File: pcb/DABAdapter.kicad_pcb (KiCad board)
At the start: 2 copper layers, 27 x 58.5 mm, 31 parts, among them J1 RFShield_OnePiece, J2 Ant, J3 Conn_01x06, J4 AudioJack3_Ground, J6 Conn_01x06, U3 abcdefg, U4 MIC5504-1.8YM5, Y1 19.2Mhz

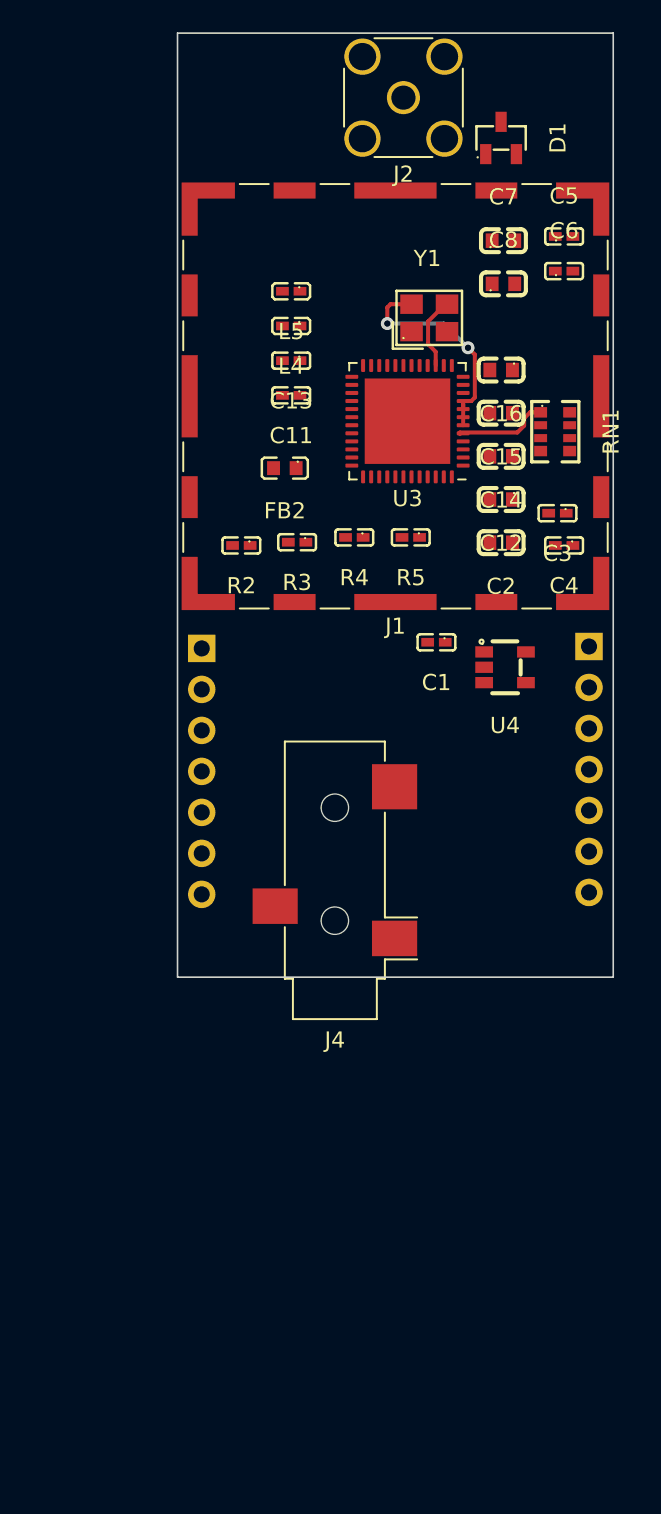
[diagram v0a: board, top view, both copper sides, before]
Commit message: Add flash chip to the layout
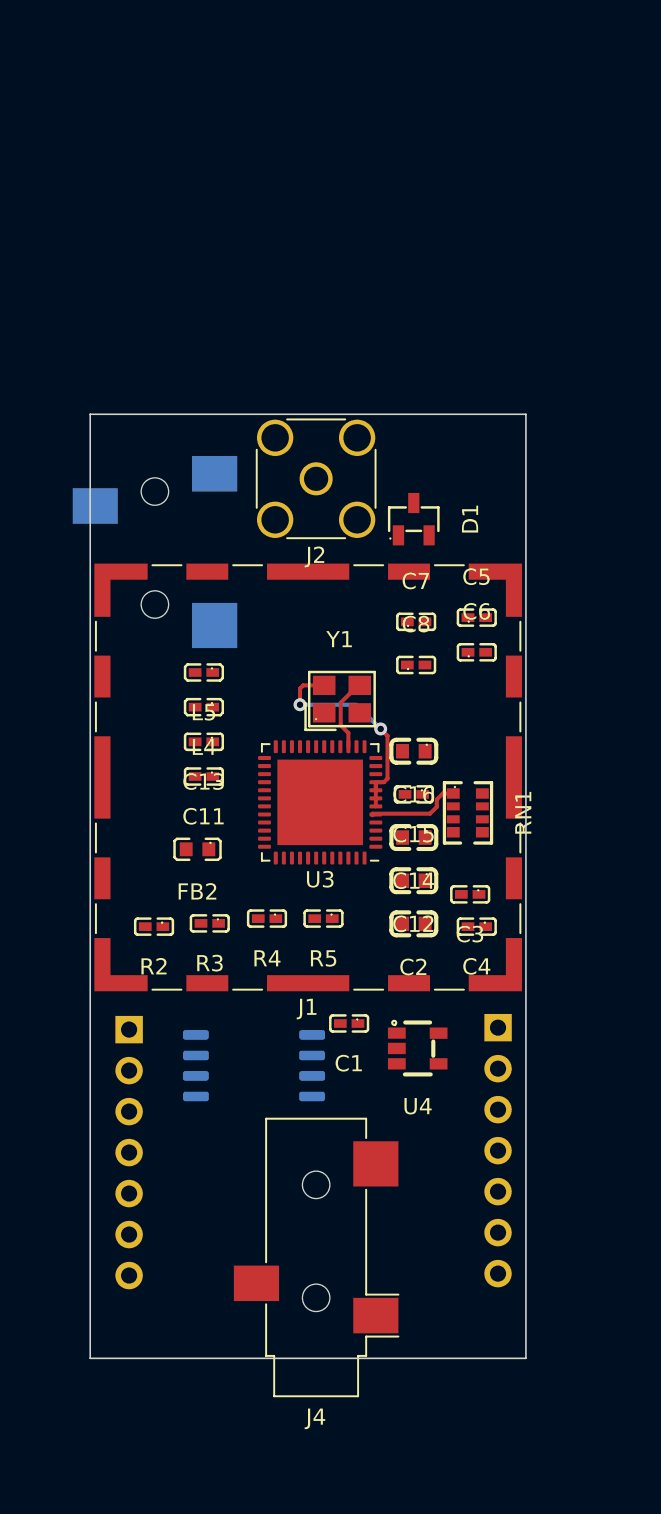
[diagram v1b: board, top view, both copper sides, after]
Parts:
- added J5: TRS Antenna, Connector_Audio:Jack_3.5mm_CUI_SJ-3523-SMT_Horizontal, B.Cu at (101.6, 69.2)
- added U1: SST25VF080B-50-4x-S2Ax, Package_SO:SOIC-8_5.275x5.275mm_P1.27mm, B.Cu at (107.7, 102.2)
- C15, C7, C8: footprint jlc_footprints:C0603 -> jlc_footprints:C0402
- moved J6 24.3 mm to (122.9, 99.9)
- moved C1 24.2 mm to (113.6, 99.6)
- moved C13 24.2 mm to (104.6, 82.2)
- moved C14 24.2 mm to (117.6, 88.1)
- moved C15 24.2 mm to (117.6, 85.4)
- moved C2 24.2 mm to (117.6, 93.4)
- moved C3 24.2 mm to (121.1, 91.6)
- moved C4 24.2 mm to (121.5, 93.6)
- moved C6 24.2 mm to (121.5, 76.6)
- moved D1 24.2 mm to (117.6, 68.4)
- moved J2 24.2 mm to (111.6, 65.9)
- moved L5 24.2 mm to (104.6, 77.9)
- moved R2 24.2 mm to (101.5, 93.6)
- moved R3 24.2 mm to (105.0, 93.4)
- moved R4 24.2 mm to (108.5, 93.1)
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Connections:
- net Net-(J2-In) renamed ANT

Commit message: Routing of the pcb
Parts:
- removed J5: TRS Antenna, Connector_Audio:Jack_3.5mm_CUI_SJ-3523-SMT_Horizontal
- removed RN1: 10k, jlc_footprints:RES-ARRAY-SMD_0603-8P-L3.2-W1.6-BL
- added R1: 10k, jlc_footprints:C0402, F.Cu at (117.7, 73.8)
- added R6: 10k, jlc_footprints:C0402, F.Cu at (122.0, 84.4)
- added R7: 10k, jlc_footprints:C0402, F.Cu at (115.6, 74.1)
- added R8: 10k, jlc_footprints:C0402, F.Cu at (115.7, 72.9)
- moved U1 27.1 mm to (115.6, 76.3), turned to 90 degrees
- moved U4 26.9 mm to (120.2, 74.4), turned to 90 degrees
- moved R2 17.9 mm to (118.6, 88.0), turned to -45 degrees
- moved C3 17.9 mm to (122.6, 73.8), turned to -90 degrees
- moved C5 17.1 mm to (111.7, 88.5), turned to 90 degrees
- moved C4 16.6 mm to (121.4, 77.0), turned to 0 degrees
- moved R3 15.8 mm to (119.5, 87.2), turned to -45 degrees
- moved J3 15.1 mm to (99.5, 115.1), turned to 0 degrees
- moved C1 14.7 mm to (110.2, 85.4), turned to 90 degrees
- moved C7 14.6 mm to (113.0, 88.5), turned to 90 degrees
- moved C6 14.0 mm to (114.3, 88.5), turned to 90 degrees
- moved R4 13.6 mm to (120.4, 86.4), turned to -45 degrees
- moved C8 13.3 mm to (110.5, 88.5), turned to 90 degrees
- moved C15 12.2 mm to (106.2, 81.2), turned to 90 degrees
- moved C2 12.1 mm to (121.4, 81.9)
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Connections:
- J3 pad 3: SMODE -> ROUT
- J3 pad 4: INTB -> LOUT
- J3 pad 5: RSTB -> INTB
- J3 pad 6: LOUT -> RSTB
- J3 pad 7: ROUT -> SMODE
- J6 pad 3: SPI_SSB -> SPI_SCLK
- J6 pad 4: SPI_SCLK -> SPI_SSB
- J6 pad 5: I2S_DCLK -> I2S_DFS
- J6 pad 6: I2S_DFS -> I2S_DCLK
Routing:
- net INTB: track 0.10 -> 54.5 mm, vias 0 -> 3
- net +3V3: track 0.00 -> 46.9 mm, vias 0 -> 6
- net RSTB: track 0.00 -> 43.6 mm, vias 0 -> 2
- net LOUT: track 0.00 -> 39.6 mm, vias 0 -> 2
- net ROUT: track 0.00 -> 37.8 mm
- net I2S_DATA: track 0.00 -> 37.3 mm
- net SMODE: track 5.89 -> 41.7 mm, vias 0 -> 2
- net I2S_DCLK: track 0.00 -> 31.6 mm
- net I2S_DFS: track 0.00 -> 29.3 mm
- net GND: track 14.1 -> 40.3 mm, vias 2 -> 34
- net SPI_SSB: track 0.00 -> 22.8 mm
- net +1V8: track 0.00 -> 21.7 mm, vias 0 -> 2
- net SPI_SCLK: track 0.00 -> 17.9 mm
- net SPI_MOSI: track 0.00 -> 16.4 mm
- net SPI_MISO: track 0.00 -> 14.8 mm
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- added copper zone on F.Cu, net +1V8
- added copper zone on F.Cu, net +3V3
- added copper zone on B.Cu, net GND
- added copper zone on F.Cu, net GND

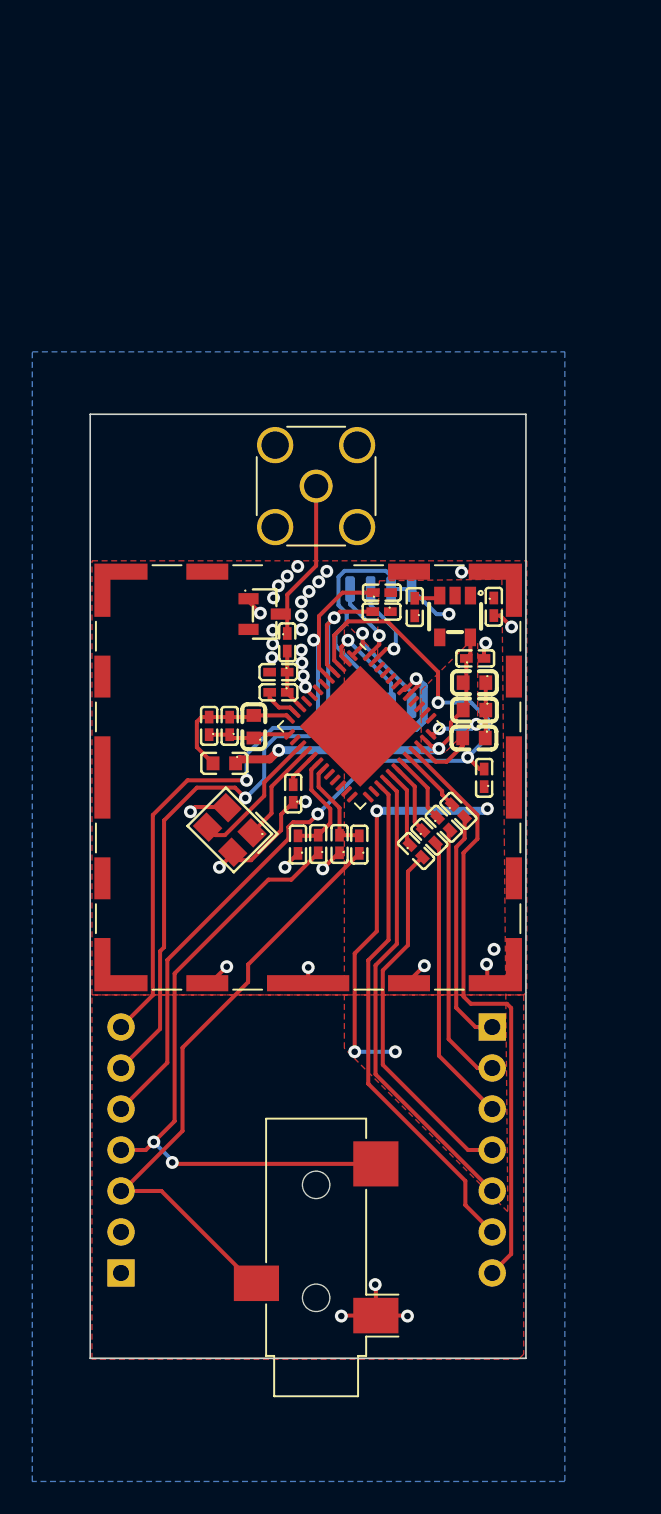
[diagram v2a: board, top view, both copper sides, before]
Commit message: DRC and add step file of QFN package
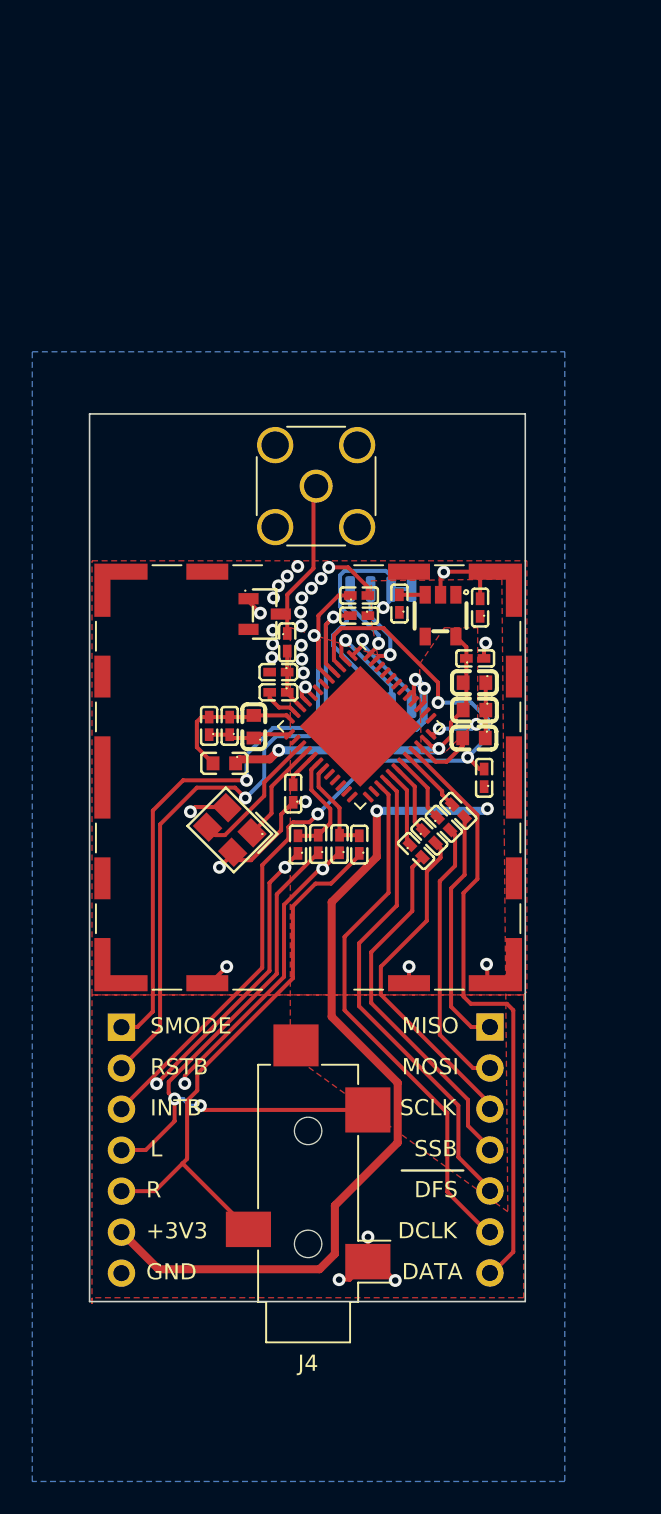
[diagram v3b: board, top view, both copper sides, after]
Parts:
- J4: footprint Connector_Audio:Jack_3.5mm_CUI_SJ-3523-SMT_Horizontal -> Connector_Audio:Jack_3.5mm_CUI_SJ-3524-SMT_Horizontal
- moved J3 15.2 mm to (99.5, 99.8), turned to 180 degrees
- moved J4 3.38 mm to (111.1, 110.8)
- moved R8 1.43 mm to (114.2, 73.1)
- moved R7 1.42 mm to (114.2, 74.3)
- moved R1 0.97 mm to (116.8, 73.6)
- moved U4 0.90 mm to (119.3, 74.3)
- moved C3 0.85 mm to (121.8, 73.8), turned to 90 degrees
- moved J6 0.14 mm to (122.4, 99.8)
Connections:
- J3 pad 1: GND -> SMODE
- J3 pad 2: +3V3 -> RSTB
- J3 pad 3: ROUT -> INTB
- J3 pad 5: INTB -> ROUT
- J3 pad 6: RSTB -> +3V3
- J3 pad 7: SMODE -> GND
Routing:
- net GND: track 40.3 -> 81.4 mm, vias 34 -> 35
- net +3V3: track 46.9 -> 73.7 mm, vias 6 -> 3
- net ROUT: track 37.8 -> 34.6 mm
- net SPI_SCLK: track 17.9 -> 21.0 mm
- net LOUT: track 39.6 -> 36.9 mm
- net I2S_DCLK: track 31.6 -> 33.0 mm
- net RSTB: track 43.6 -> 42.2 mm
- net SPI_MOSI: track 16.4 -> 17.3 mm
- net I2S_DFS: track 29.3 -> 30.1 mm
- net NVSSB: track 7.36 -> 6.55 mm
- net INTB: track 54.5 -> 53.8 mm
- net SMODE: track 41.7 -> 42.3 mm
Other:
- board size 27 x 58.5 mm -> 27 x 55 mm

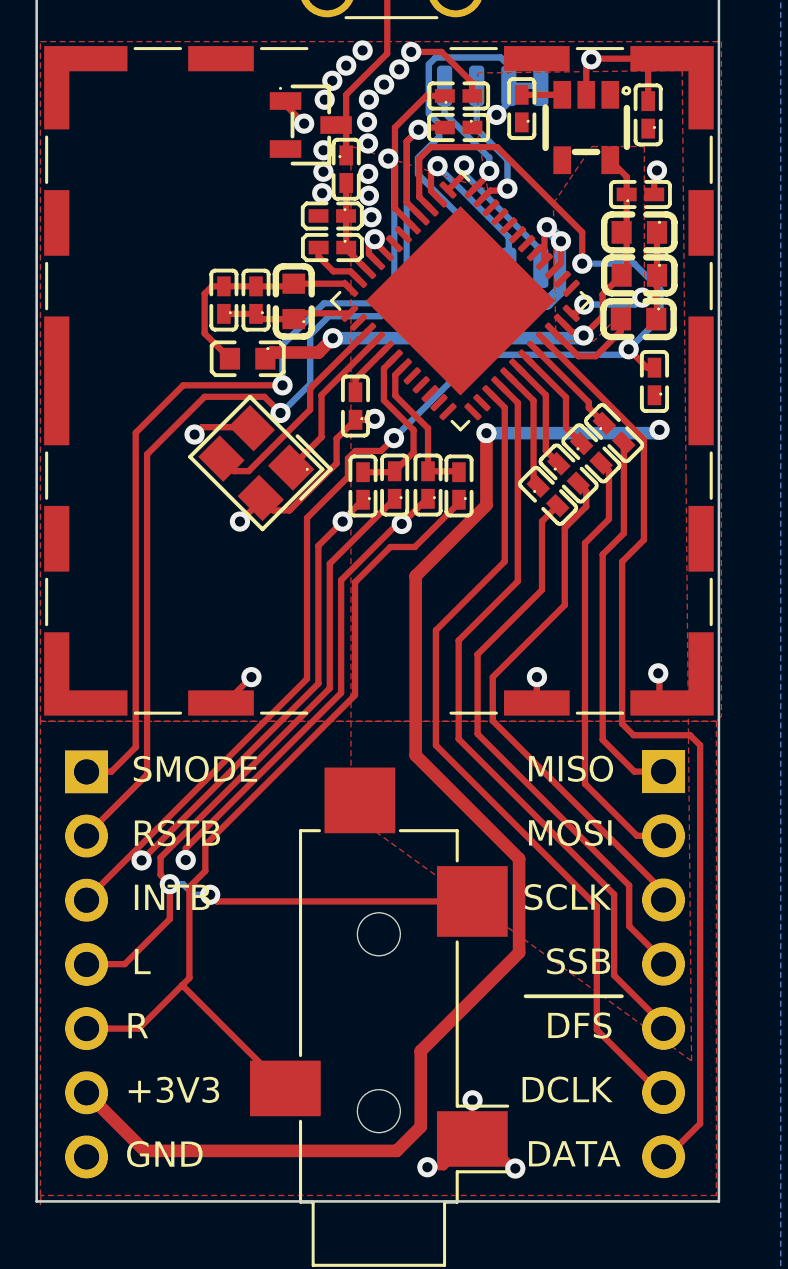
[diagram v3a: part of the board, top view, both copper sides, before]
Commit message: Rename FS to RLCLK
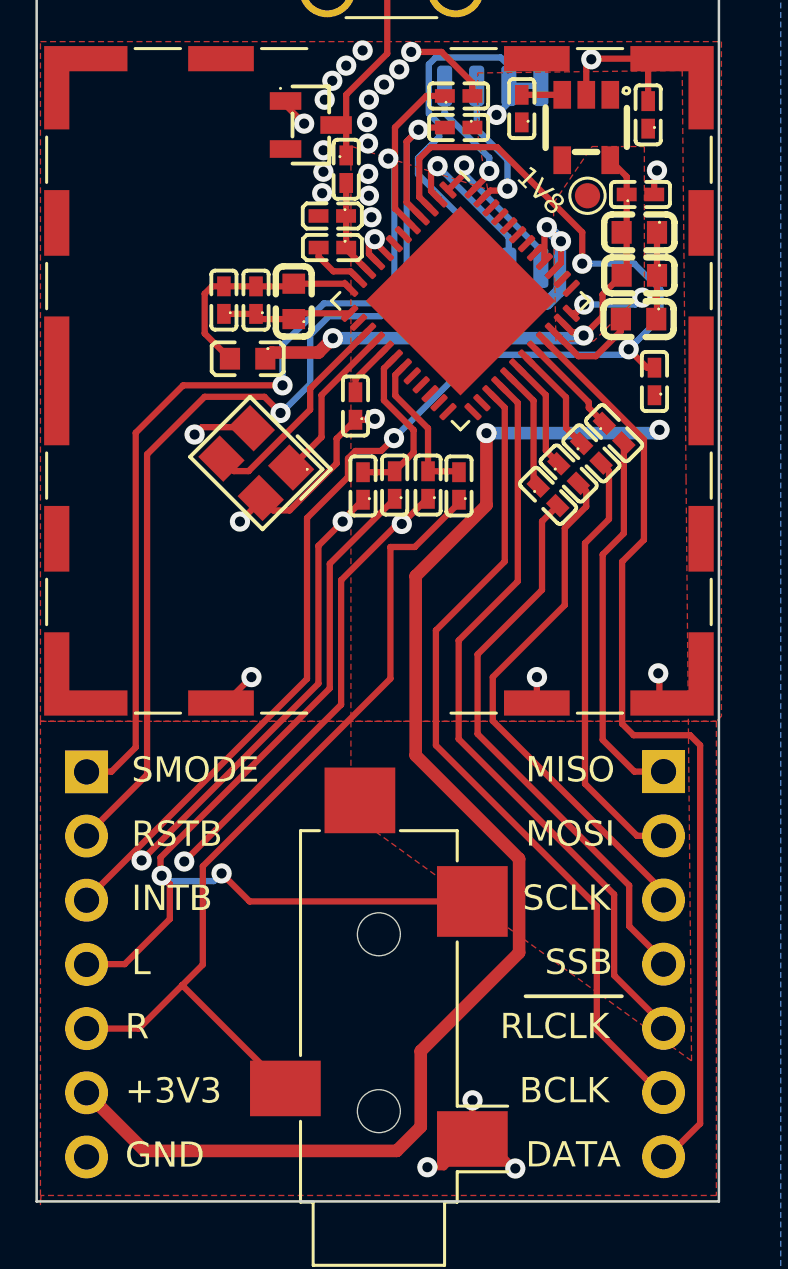
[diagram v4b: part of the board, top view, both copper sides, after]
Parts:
- added TP2: 1V8, TestPoint:TestPoint_Pad_D1.0mm, F.Cu at (119.3, 77.0)
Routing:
- net LOUT: track 36.9 -> 38.1 mm

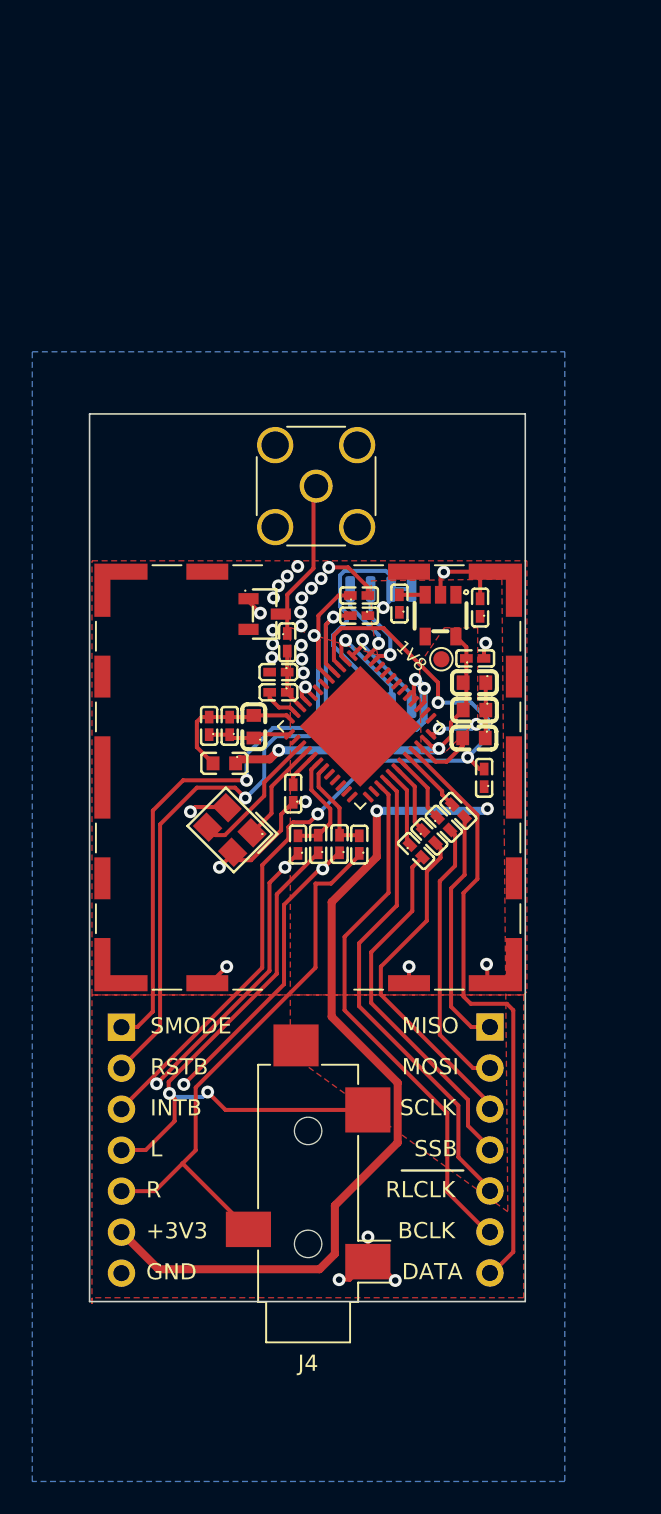
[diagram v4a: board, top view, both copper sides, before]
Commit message: Finishing touches
- Added image to readme
- Add Wuerth 3d model of the shield
- Add DAB logo to the pcb
- New board outline for the optional TRS antenna socket
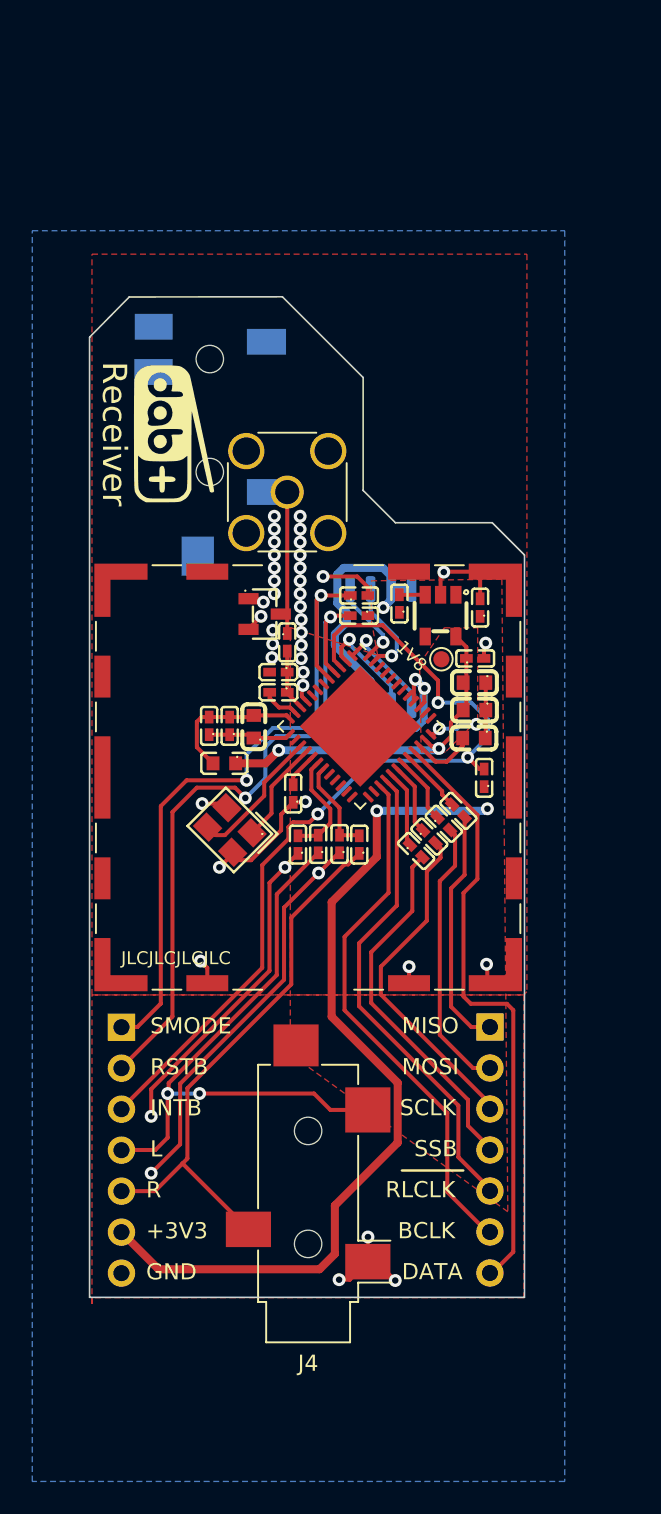
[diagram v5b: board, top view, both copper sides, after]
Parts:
- added G***: LOGO, LOGO, F.Cu at (102.8, 63.1)
- added G***: LOGO, LOGO, B.Cu at (102.9, 92.7)
- added J7: AudioJack3_SwitchTR, Connector_Audio:Jack_3.5mm_CUI_SJ2-3593D-SMT_Horizontal, B.Cu at (105.0, 61.0)
- moved J2 1.83 mm to (109.8, 66.7)
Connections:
- net I2S_DFS renamed I2S_RLCLK
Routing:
- net GND: track 81.5 -> 91.7 mm, vias 35 -> 44
- net SMODE: track 42.3 -> 43.3 mm
- net ANT: track 10.3 -> 11.3 mm
- net LOUT: track 38.1 -> 37.6 mm
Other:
- board size 27 x 55 mm -> 27 x 62 mm
- board text added: "JLCJLCJLCJLC"
- board text added: "Receiver"
